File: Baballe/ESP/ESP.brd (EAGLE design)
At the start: 30 x 32 mm, 8 parts

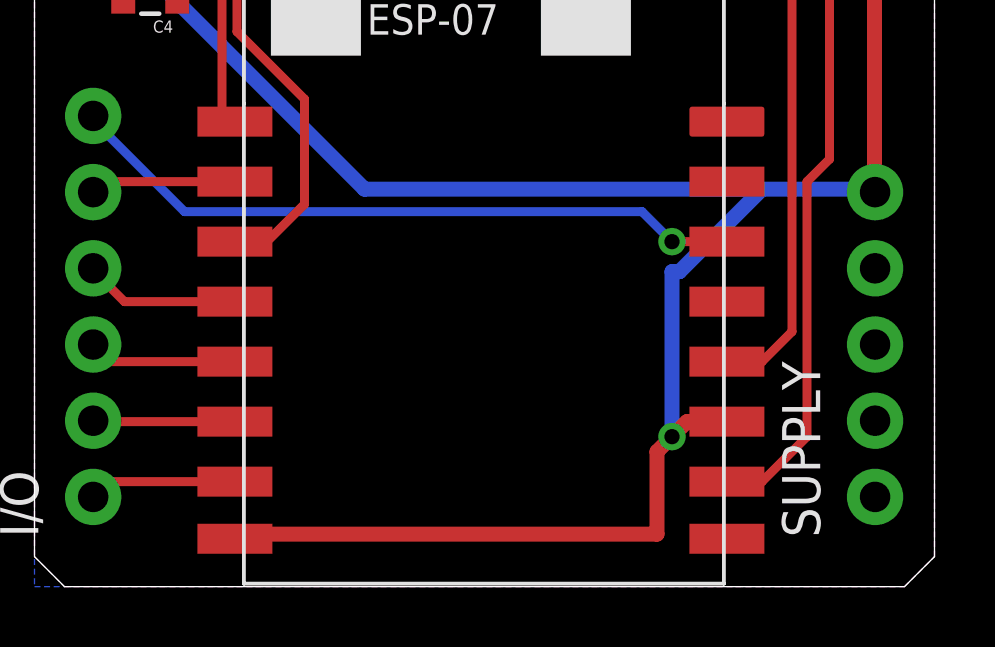
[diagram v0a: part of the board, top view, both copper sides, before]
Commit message: Modification sur les modules led et alimentation
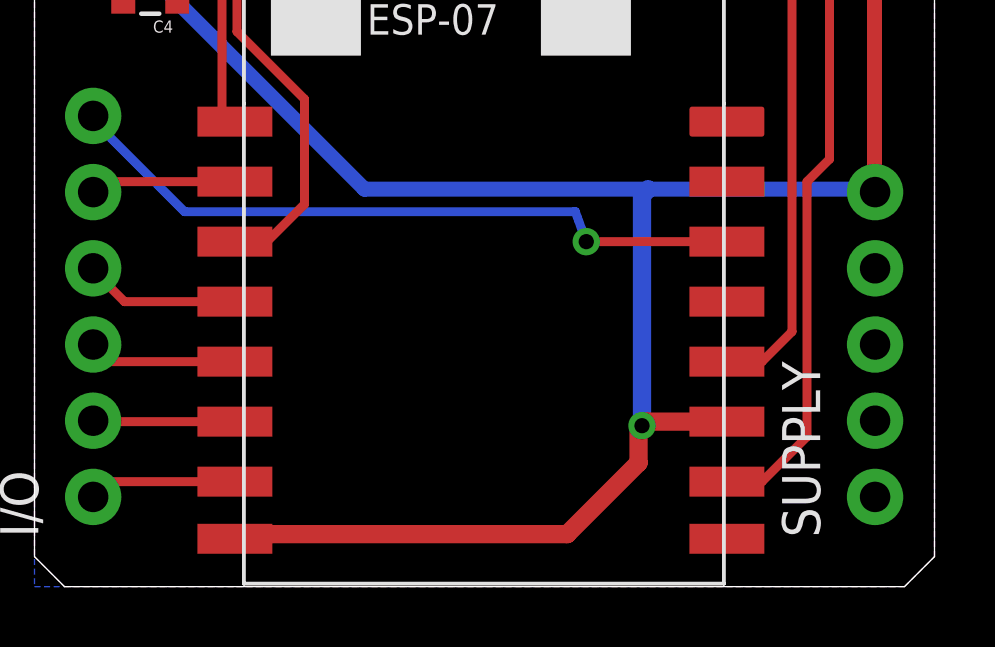
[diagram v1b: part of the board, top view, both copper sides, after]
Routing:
- net VCC: track 76.8 -> 74.2 mm
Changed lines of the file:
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@@
 <setting verticaltext="up"/>
 </settings>
-<grid distance="1" unitdist="mm" unit="mm" style="lines" multiple="1" display="yes" altdistance="0.025" altunitdist="inch" altunit="inch"/>
+<grid distance="12.5" unitdist="mil" unit="mil" style="lines" multiple="1" display="yes" altdistance="0.025" altunitdist="inch" altunit="inch"/>
 <layers>
 <layer number="1" name="Top" color="4" fill="1" visible="yes" active="yes"/>
@@
 <contactref element="C4" pad="2"/>
 <contactref element="SUPPLY" pad="5"/>
-<wire x1="64.75" y1="1.75" x2="50.75" y2="1.75" width="0.5" layer="1"/>
-<wire x1="64.75" y1="4.5" x2="64.75" y2="1.75" width="0.5" layer="1"/>
-<wire x1="65.75" y1="5.5" x2="65.25" y2="5" width="0.5" layer="1"/>
-<wire x1="65.25" y1="5" x2="64.75" y2="4.5" width="0.5" layer="1"/>
-<wire x1="67.08" y1="5.5" x2="65.75" y2="5.5" width="0.5" layer="1"/>
 <wire x1="50.75" y1="1.75" x2="50.68" y2="1.595" width="0.5" layer="1"/>
 <wire x1="47" y1="27" x2="47" y2="24.25" width="0.5" layer="1"/>
@@
 <wire x1="72" y1="13.25" x2="72.0188625" y2="13.151" width="0.5" layer="1"/>
 <wire x1="55" y1="13.25" x2="47" y2="21.25" width="0.5" layer="16"/>
-<wire x1="72" y1="13.25" x2="68.25" y2="13.25" width="0.5" layer="16"/>
-<wire x1="68.25" y1="13.25" x2="55" y2="13.25" width="0.5" layer="16"/>
+<wire x1="72" y1="13.25" x2="64.4525" y2="13.25" width="0.5" layer="16"/>
+<wire x1="64.4525" y1="13.25" x2="55" y2="13.25" width="0.5" layer="16"/>
 <wire x1="72" y1="13.25" x2="72.0188625" y2="13.151" width="0.5" layer="16"/>
-<wire x1="65.25" y1="10.5" x2="65.25" y2="5" width="0.5" layer="16"/>
-<wire x1="65.5" y1="10.5" x2="65.25" y2="10.5" width="0.5" layer="16"/>
-<wire x1="68.25" y1="13.25" x2="65.5" y2="10.5" width="0.5" layer="16"/>
 <via x="47" y="21.25" extent="1-16" drill="0.508"/>
-<via x="65.25" y="5" extent="1-16" drill="0.508"/>
+<via x="64.25" y="5.365" extent="1-16" drill="0.508"/>
+<wire x1="67.08" y1="5.5" x2="64.385" y2="5.5" width="0.6096" layer="1"/>
+<wire x1="64.385" y1="5.5" x2="64.25" y2="5.365" width="0.6096" layer="1"/>
+<wire x1="64.25" y1="5.365" x2="64.25" y2="13.0475" width="0.6096" layer="16"/>
+<wire x1="64.25" y1="13.0475" x2="64.4525" y2="13.25" width="0.6096" layer="16"/>
+<wire x1="50.75" y1="1.75" x2="61.7575" y2="1.75" width="0.6096" layer="1"/>
+<wire x1="61.7575" y1="1.75" x2="64.135" y2="4.1275" width="0.6096" layer="1"/>
+<wire x1="64.135" y1="4.1275" x2="64.135" y2="5.25" width="0.6096" layer="1"/>
+<wire x1="64.135" y1="5.25" x2="64.25" y2="5.365" width="0.6096" layer="1"/>
 </signal>
 <signal name="N$1">
@@
 <contactref element="I/O" pad="6"/>
 <contactref element="U$1" pad="GPIO4"/>
-<wire x1="65.25" y1="11.5" x2="67.08" y2="11.5" width="0.3" layer="1"/>
-<wire x1="64.25" y1="12.5" x2="65.25" y2="11.5" width="0.3" layer="16"/>
-<wire x1="49" y1="12.5" x2="64.25" y2="12.5" width="0.3" layer="16"/>
+<wire x1="62.3925" y1="11.5" x2="67.08" y2="11.5" width="0.3" layer="1"/>
+<wire x1="62.0275" y1="12.5" x2="62.3925" y2="11.5" width="0.3" layer="16"/>
+<wire x1="49" y1="12.5" x2="62.0275" y2="12.5" width="0.3" layer="16"/>
 <wire x1="46" y1="15.5" x2="49" y2="12.5" width="0.3" layer="16"/>
 <wire x1="46" y1="15.5" x2="45.95533125" y2="15.691" width="0.3" layer="16"/>
-<via x="65.25" y="11.5" extent="1-16" drill="0.508"/>
+<via x="62.3925" y="11.5" extent="1-16" drill="0.508"/>
 </signal>
 </signals>

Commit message: V2 de la Baballe
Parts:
- moved C4 42.5 mm to (7.68, 33.4)
- moved SUPPLY 40.8 mm to (31.8, 10.3)
- moved R7 40.4 mm to (7.82, 30.1)
- moved R8 40.0 mm to (7.86, 26.9)
- moved R5 39.5 mm to (31.4, 33.1)
- moved R6 39.4 mm to (31.3, 30.1)
- moved U$1 39.2 mm to (19.9, 13.7)
- moved I/O 38.5 mm to (8.13, 10.3)
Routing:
- net N$1: track 26.0 -> 39.1 mm, vias 0 -> 2
- net VCC: track 74.2 -> 81.9 mm, vias 2 -> 4
- net I_BUTTON: track 5.21 -> 10.0 mm, vias 0 -> 1
- net N$10: track 20.1 -> 15.5 mm
- net N$6: track 18.6 -> 23.1 mm
- net O_BLUE: track 5.26 -> 9.78 mm, vias 0 -> 1
- net N$9: track 10.4 -> 12.9 mm
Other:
- board size 30 x 32 mm -> 40 x 40 mm

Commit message: Baballe en attente de vérification finale
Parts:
- moved I/O 0.36 mm to (7.93, 9.96)
- moved SUPPLY 0.34 mm to (32.0, 9.96)
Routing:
- net O_GREEN: track 5.30 -> 4.78 mm
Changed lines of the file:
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@@
 <board>
 <plain>
-<wire x1="40" y1="22" x2="32" y2="22" width="0.1" layer="47"/>
-<wire x1="32" y1="22" x2="8" y2="22" width="0.1" layer="47"/>
-<wire x1="8" y1="22" x2="0" y2="22" width="0.1" layer="47"/>
 <wire x1="20" y1="42" x2="20" y2="2" width="0.1" layer="47"/>
 <circle x="20" y="22" radius="20" width="0.1" layer="20"/>
-<wire x1="32" y1="22" x2="32" y2="19" width="0.1" layer="47"/>
-<wire x1="8" y1="22" x2="8" y2="20" width="0.1" layer="47"/>
 <hole x="20" y="34" drill="15"/>
-<wire x1="4" y1="34" x2="36" y2="34" width="0.1" layer="47"/>
 </plain>
 <attributes>
@@
 <attribute name="DIMENSIONS" value="22.0 x 16.0 mm" x="19.88" y="13.7" size="1.778" layer="27" display="off"/>
 </element>
-<element name="I/O" library="SparkFun-Connectors" package="1X06_NO_SILK" value="I/O" x="8.12533125" y="10.261" rot="R90">
-<attribute name="PROD_ID" value="CONN-08437" x="8.12533125" y="10.261" size="1.778" layer="27" rot="R90" display="off"/>
+<element name="I/O" library="SparkFun-Connectors" package="1X06_NO_SILK" value="I/O" x="7.92533125" y="9.961" rot="R90">
+<attribute name="PROD_ID" value="CONN-08437" x="7.92533125" y="9.961" size="1.778" layer="27" rot="R90" display="off"/>
 </element>
-<element name="SUPPLY" library="SparkFun-Connectors" package="1X05_NO_SILK" value="SUPPLY" x="31.8488625" y="10.261" rot="R90"/>
+<element name="SUPPLY" library="SparkFun-Connectors" package="1X05_NO_SILK" value="SUPPLY" x="31.9988625" y="9.961" rot="R90"/>
 </elements>
 <signals>
@@
 <wire x1="32" y1="20.5" x2="33.5" y2="20.5" width="0.5" layer="16"/>
 <wire x1="32.5" y1="30" x2="32.24105625" y2="30.101309375" width="0.5" layer="1"/>
-<wire x1="32" y1="20.5" x2="31.8488625" y2="20.421" width="0.5" layer="16"/>
+<wire x1="32" y1="20.5" x2="31.9988625" y2="20.121" width="0.5" layer="16"/>
 <wire x1="14" y1="5.5" x2="12" y2="5.5" width="0.5" layer="1"/>
 <wire x1="23" y1="14.5" x2="14" y2="5.5" width="0.5" layer="16"/>
@@
 <wire x1="32" y1="20" x2="26.5" y2="14.5" width="0.5" layer="16"/>
 <wire x1="12" y1="5.5" x2="11.68" y2="5.595" width="0.5" layer="1"/>
-<wire x1="32" y1="20" x2="31.8488625" y2="20.421" width="0.5" layer="16"/>
+<wire x1="32" y1="20" x2="31.9988625" y2="20.121" width="0.5" layer="16"/>
 <wire x1="25" y1="9.5" x2="28.08" y2="9.5" width="0.5" layer="1"/>
 <wire x1="25" y1="14.5" x2="25" y2="9.5" width="0.5" layer="16"/>
@@
 <wire x1="36" y1="30.5" x2="33.5" y2="33" width="0.3" layer="16"/>
 <wire x1="36" y1="12.5" x2="36" y2="30.5" width="0.3" layer="16"/>
-<wire x1="31.5" y1="8" x2="36" y2="12.5" width="0.3" layer="16"/>
-<wire x1="24.92" y1="8" x2="31.5" y2="8" width="0.3" layer="16"/>
+<wire x1="32.5" y1="8" x2="36" y2="12.5" width="0.3" layer="16"/>
+<wire x1="24.92" y1="8" x2="32.5" y2="8" width="0.3" layer="16"/>
 <wire x1="32.5" y1="33" x2="32.27745625" y2="33.112346875" width="0.3" layer="1"/>
 <via x="33.5" y="33" extent="1-16" drill="0.6096"/>
@@
 <contactref element="U$1" pad="GPIO13"/>
 <contactref element="I/O" pad="1"/>
-<wire x1="10" y1="7.5" x2="11.68" y2="7.5" width="0.3" layer="1"/>
-<wire x1="8" y1="9.5" x2="10" y2="7.5" width="0.3" layer="1"/>
-<wire x1="8" y1="10" x2="8" y2="9.5" width="0.3" layer="1"/>
-<wire x1="8" y1="10" x2="8.12533125" y2="10.261" width="0.3" layer="1"/>
+<wire x1="10.3412" y1="7.53" x2="11.6464" y2="7.53" width="0.3" layer="1"/>
+<wire x1="7.9316" y1="9.9396" x2="10.3412" y2="7.53" width="0.3" layer="1"/>
+<wire x1="11.6464" y1="7.53" x2="11.68" y2="7.5" width="0.3" layer="1"/>
+<wire x1="7.9316" y1="9.9396" x2="7.92533125" y2="9.961" width="0.3" layer="1"/>
 </signal>
 <signal name="O_BLUE">
@@
 <wire x1="10.5" y1="15" x2="14" y2="11.5" width="0.3" layer="16"/>
 <wire x1="8.5" y1="15" x2="10.5" y2="15" width="0.3" layer="16"/>
-<wire x1="8.5" y1="15" x2="8.12533125" y2="15.341" width="0.3" layer="16"/>
+<wire x1="8.5" y1="15" x2="7.92533125" y2="15.041" width="0.3" layer="16"/>
 <via x="14" y="11.5" extent="1-16" drill="0.6096"/>
 </signal>
@@
 <wire x1="10" y1="17.5" x2="14" y2="13.5" width="0.3" layer="16"/>
 <wire x1="8.5" y1="17.5" x2="10" y2="17.5" width="0.3" layer="16"/>
-<wire x1="8.5" y1="17.5" x2="8.12533125" y2="17.881" width="0.3" layer="16"/>
+<wire x1="8.5" y1="17.5" x2="7.92533125" y2="17.581" width="0.3" layer="16"/>
 <via x="14" y="13.5" extent="1-16" drill="0.6096"/>
 </signal>
@@
 <wire x1="8.5" y1="12.5" x2="11.5" y2="9.5" width="0.3" layer="1"/>
 <wire x1="11.5" y1="9.5" x2="11.68" y2="9.5" width="0.3" layer="1"/>
-<wire x1="8.5" y1="12.5" x2="8.12533125" y2="12.801" width="0.3" layer="1"/>
+<wire x1="8.5" y1="12.5" x2="7.92533125" y2="12.501" width="0.3" layer="1"/>
 </signal>
 <signal name="I_VBAT">
 <contactref element="U$1" pad="ADC"/>
 <contactref element="I/O" pad="5"/>
-<wire x1="8.5" y1="20.5" x2="11.5" y2="17.5" width="0.3" layer="1"/>
+<wire x1="7.865" y1="19.23" x2="11.5" y2="17.5" width="0.3" layer="1"/>
 <wire x1="11.5" y1="17.5" x2="11.68" y2="17.5" width="0.3" layer="1"/>
-<wire x1="8.5" y1="20.5" x2="8.12533125" y2="20.421" width="0.3" layer="1"/>
+<wire x1="7.865" y1="19.23" x2="7.92533125" y2="20.121" width="0.3" layer="1"/>
 </signal>
 <signal name="O_POWER_CTRL">
@@
 <wire x1="19" y1="22.5" x2="26" y2="15.5" width="0.3" layer="16"/>
 <wire x1="8.5" y1="22.5" x2="19" y2="22.5" width="0.3" layer="16"/>
-<wire x1="8.5" y1="22.5" x2="8.12533125" y2="22.961" width="0.3" layer="16"/>
+<wire x1="8.5" y1="22.5" x2="7.92533125" y2="22.661" width="0.3" layer="16"/>
 <via x="26" y="15.5" extent="1-16" drill="0.6096"/>
 </signal>
